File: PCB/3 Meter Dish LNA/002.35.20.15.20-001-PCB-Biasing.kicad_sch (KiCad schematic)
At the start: 7 parts, among them U1 PMA2-63LN+

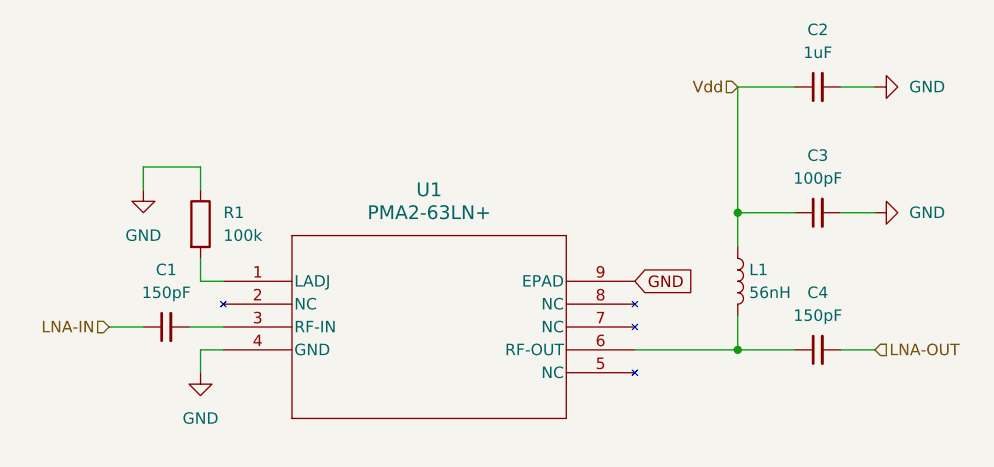
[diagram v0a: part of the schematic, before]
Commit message: Added document numbers
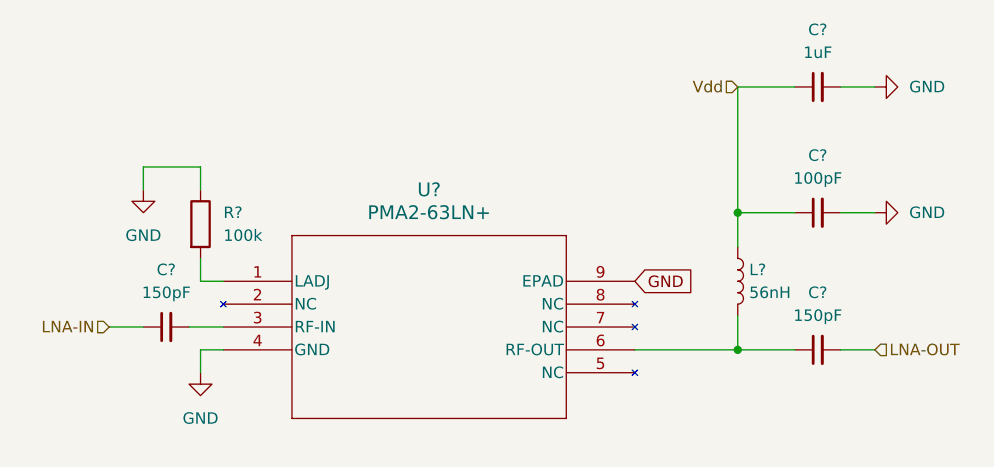
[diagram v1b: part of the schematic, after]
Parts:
- renumbered C2 to C?, C3 to C?, C4 to C?, C1 to C?, L1 to L?, R1 to R?, U1 to U?
